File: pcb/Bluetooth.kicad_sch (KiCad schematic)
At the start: 17 parts, among them U13 RN4678, U14 TXB0102DCU

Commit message: [pcb] Footprints assigned
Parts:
- C26: footprint (none) -> Capacitor_Tantalum_SMD:CP_EIA-3216-18_Kemet-A
- C27, C28, C29: footprint (none) -> Capacitor_SMD:C_0805_2012Metric
- D8: footprint (none) -> LED_SMD:LED_0805_2012Metric
- JP1, JP2, JP3, JP4, JP5, JP6: footprint (none) -> Connector_PinHeader_2.54mm:PinHeader_1x02_P2.54mm_Vertical
- R38, R39: footprint (none) -> Resistor_SMD:R_0805_2012Metric
- TP18, TP19: footprint (none) -> TestPoint:TestPoint_Pad_D2.0mm
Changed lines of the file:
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@@
       (effects (font (size 1.27 1.27)) hide)
     )
-    (property "Footprint" "" (at 93.98 64.77 0)
+    (property "Footprint" "Connector_PinHeader_2.54mm:PinHeader_1x02_P2.54mm_Vertical" (at 93.98 64.77 0)
       (effects (font (size 1.27 1.27)) hide)
     )
@@
       (effects (font (size 1.27 1.27)) (justify right) hide)
     )
-    (property "Footprint" "" (at 64.77 93.98 0)
+    (property "Footprint" "Connector_PinHeader_2.54mm:PinHeader_1x02_P2.54mm_Vertical" (at 64.77 93.98 0)
       (effects (font (size 1.27 1.27)) hide)
     )
@@
       (effects (font (size 1.27 1.27)) hide)
     )
-    (property "Footprint" "" (at 182.88 68.58 0)
+    (property "Footprint" "Connector_PinHeader_2.54mm:PinHeader_1x02_P2.54mm_Vertical" (at 182.88 68.58 0)
       (effects (font (size 1.27 1.27)) hide)
     )
@@
       (effects (font (size 1.27 1.27)) (justify right))
     )
-    (property "Footprint" "" (at 140.6652 53.34 0)
+    (property "Footprint" "Capacitor_SMD:C_0805_2012Metric" (at 140.6652 53.34 0)
       (effects (font (size 1.27 1.27)) hide)
     )
@@
       (effects (font (size 1.27 1.27)))
     )
-    (property "Footprint" "" (at 93.98 52.07 0)
+    (property "Footprint" "LED_SMD:LED_0805_2012Metric" (at 93.98 52.07 0)
       (effects (font (size 1.27 1.27)) hide)
     )
@@
       (effects (font (size 1.27 1.27)) (justify right) hide)
     )
-    (property "Footprint" "" (at 67.31 93.98 0)
+    (property "Footprint" "Connector_PinHeader_2.54mm:PinHeader_1x02_P2.54mm_Vertical" (at 67.31 93.98 0)
       (effects (font (size 1.27 1.27)) hide)
     )
@@
       (effects (font (size 1.27 1.27)) (justify left))
     )
-    (property "Footprint" "" (at 91.1352 104.14 0)
+    (property "Footprint" "Capacitor_SMD:C_0805_2012Metric" (at 91.1352 104.14 0)
       (effects (font (size 1.27 1.27)) hide)
     )
@@
       (effects (font (size 1.27 1.27)) (justify left) hide)
     )
-    (property "Footprint" "" (at 181.61 67.31 0)
+    (property "Footprint" "TestPoint:TestPoint_Pad_D2.0mm" (at 181.61 67.31 0)
       (effects (font (size 1.27 1.27)) hide)
     )
@@
       (effects (font (size 1.27 1.27)) (justify left))
     )
-    (property "Footprint" "" (at 168.6052 60.96 0)
+    (property "Footprint" "Capacitor_SMD:C_0805_2012Metric" (at 168.6052 60.96 0)
       (effects (font (size 1.27 1.27)) hide)
     )
@@
       (effects (font (size 1.27 1.27)))
     )
-    (property "Footprint" "" (at 50.8 93.218 90)
+    (property "Footprint" "Resistor_SMD:R_0805_2012Metric" (at 50.8 93.218 90)
       (effects (font (size 1.27 1.27)) hide)
     )
@@
       (effects (font (size 1.27 1.27)) (justify left) hide)
     )
-    (property "Footprint" "" (at 171.45 74.93 0)
+    (property "Footprint" "TestPoint:TestPoint_Pad_D2.0mm" (at 171.45 74.93 0)
       (effects (font (size 1.27 1.27)) hide)
     )
@@
       (effects (font (size 1.27 1.27)) (justify left))
     )
-    (property "Footprint" "" (at 88.392 90.17 90)
+    (property "Footprint" "Resistor_SMD:R_0805_2012Metric" (at 88.392 90.17 90)
       (effects (font (size 1.27 1.27)) hide)
     )
@@
       (effects (font (size 1.27 1.27)) hide)
     )
-    (property "Footprint" "" (at 182.88 73.66 0)
+    (property "Footprint" "Connector_PinHeader_2.54mm:PinHeader_1x02_P2.54mm_Vertical" (at 182.88 73.66 0)
       (effects (font (size 1.27 1.27)) hide)
     )
@@
       (effects (font (size 1.27 1.27)) (justify right) hide)
     )
-    (property "Footprint" "" (at 69.85 93.98 0)
+    (property "Footprint" "Connector_PinHeader_2.54mm:PinHeader_1x02_P2.54mm_Vertical" (at 69.85 93.98 0)
       (effects (font (size 1.27 1.27)) hide)
     )
@@
       (effects (font (size 1.27 1.27)) (justify left))
     )
-    (property "Footprint" "" (at 26.9748 55.88 0)
-      (effects (font (size 1.27 1.27)) hide)
-    )
+    (property "Footprint" "Capacitor_Tantalum_SMD:CP_EIA-3216-18_Kemet-A" (at 26.9748 55.88 0)
+      (effects (font (size 1.27 1.27)) hide)
+    )

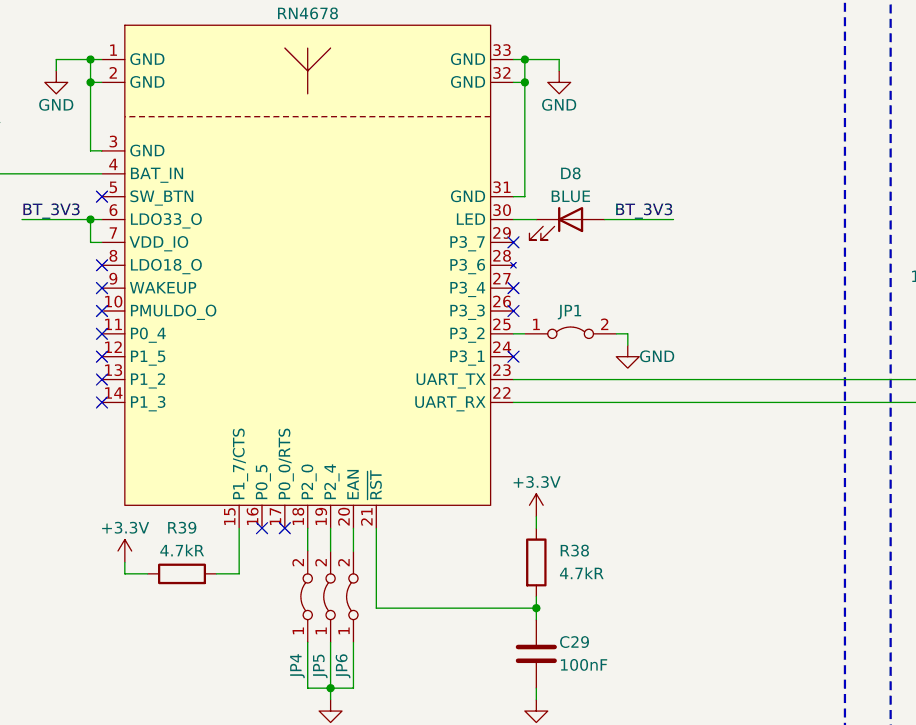
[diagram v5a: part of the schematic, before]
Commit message: [pcb] Add 100R resistor for BT status LED
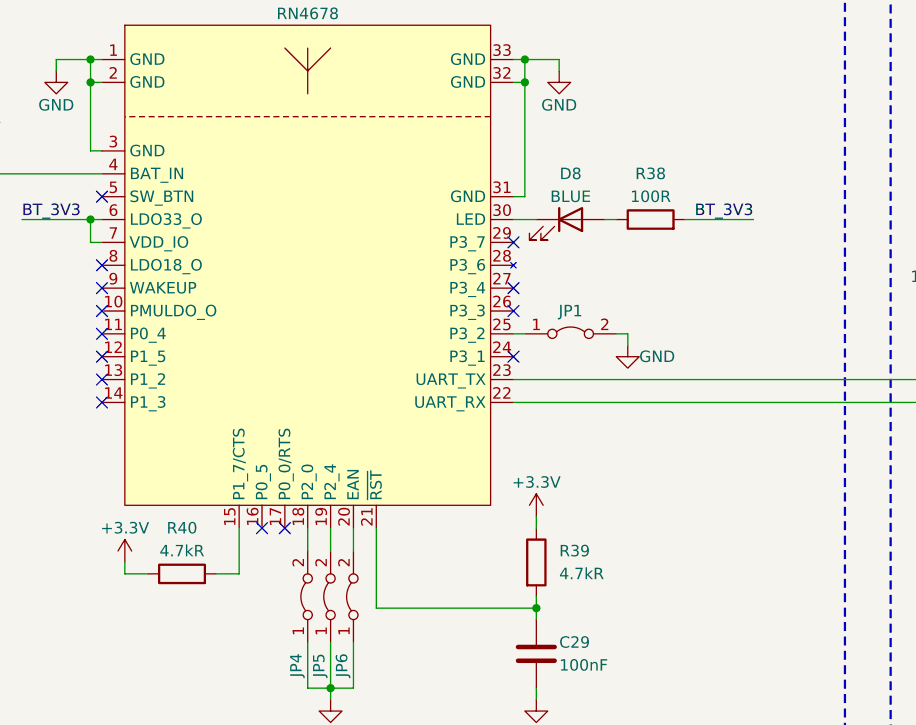
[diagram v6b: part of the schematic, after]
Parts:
- added R38: 100R, Resistor_SMD:R_0805_2012Metric, symbol Device:R
- renumbered R38 to R39, R39 to R40
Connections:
- net BT_3V3: now also R38.2; no longer D8.2 (A)
- new net: D8.2 (A), R38.1
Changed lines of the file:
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@@
+    (stroke (width 0) (type default))
+  )
+  (wire (pts (xy 106.68 52.07) (xy 114.3 52.07))
     (stroke (width 0) (type default))
   )
@@
     (stroke (width 0) (type default))
   )
-  (wire (pts (xy 97.79 52.07) (xy 105.41 52.07))
-    (stroke (width 0) (type default))
-  )
   (wire (pts (xy 36.83 35.56) (xy 36.83 34.29))
     (stroke (width 0) (type default))
@@
   )
   (wire (pts (xy 87.63 49.53) (xy 88.9 49.53))
+    (stroke (width 0) (type default))
+  )
+  (wire (pts (xy 97.79 52.07) (xy 99.06 52.07))
     (stroke (width 0) (type default))
   )
@@
     (effects (font (size 2 2) (thickness 0.4) bold) (justify left bottom))
   )
-  (label "BT_3V3" (at 105.41 52.07 180) (fields_autoplaced)
+  (label "BT_3V3" (at 114.3 52.07 180) (fields_autoplaced)
     (effects (font (size 1.27 1.27)) (justify right bottom))
   )
@@
     )
   )
+  (symbol (lib_id "Device:R") (at 102.87 52.07 90) (unit 1)
+    (in_bom yes) (on_board yes) (dnp no)
+    (property "Reference" "R38" (at 102.87 46.99 90)
+      (effects (font (size 1.27 1.27)))
+    )
+    (property "Value" "100R" (at 102.87 49.53 90)
+      (effects (font (size 1.27 1.27)))
+    )
+    (property "Footprint" "Resistor_SMD:R_0805_2012Metric" (at 102.87 53.848 90)
+      (effects (font (size 1.27 1.27)) hide)
+    )
+    (property "Datasheet" "~" (at 102.87 52.07 0)
+      (effects (font (size 1.27 1.27)) hide)
+    )
+    (pin "1")
+    (pin "2")
+    (instances
+      (project "Autko"
+        (path "/8d5cfdec-de34-4148-9100-7125640c46f5/bb9a200c-6921-438f-a82b-708524bb5612"
+          (reference "R38") (unit 1)
+        )
+      )
+    )
+  )
   (symbol (lib_id "power:GND") (at 139.7 62.23 0) (unit 1)
     (in_bom yes) (on_board yes) (dnp no)
@@
   (symbol (lib_id "Device:R") (at 50.8 91.44 90) (unit 1)
     (in_bom yes) (on_board yes) (dnp no)
-    (property "Reference" "R39" (at 50.8 86.36 90)
+    (property "Reference" "R40" (at 50.8 86.36 90)
       (effects (font (size 1.27 1.27)))
     )
@@
       (project "Autko"
         (path "/8d5cfdec-de34-4148-9100-7125640c46f5/bb9a200c-6921-438f-a82b-708524bb5612"
-          (reference "R39") (unit 1)
+          (reference "R40") (unit 1)
         )
       )
@@
   (symbol (lib_id "Device:R") (at 90.17 90.17 0) (unit 1)
     (in_bom yes) (on_board yes) (dnp no)
-    (property "Reference" "R38" (at 92.71 88.9 0)
+    (property "Reference" "R39" (at 92.71 88.9 0)
       (effects (font (size 1.27 1.27)) (justify left))
     )
@@
       (project "Autko"
         (path "/8d5cfdec-de34-4148-9100-7125640c46f5/bb9a200c-6921-438f-a82b-708524bb5612"
-          (reference "R38") (unit 1)
-        )
-      )
+          (reference "R39") (unit 1)
+        )
+      )

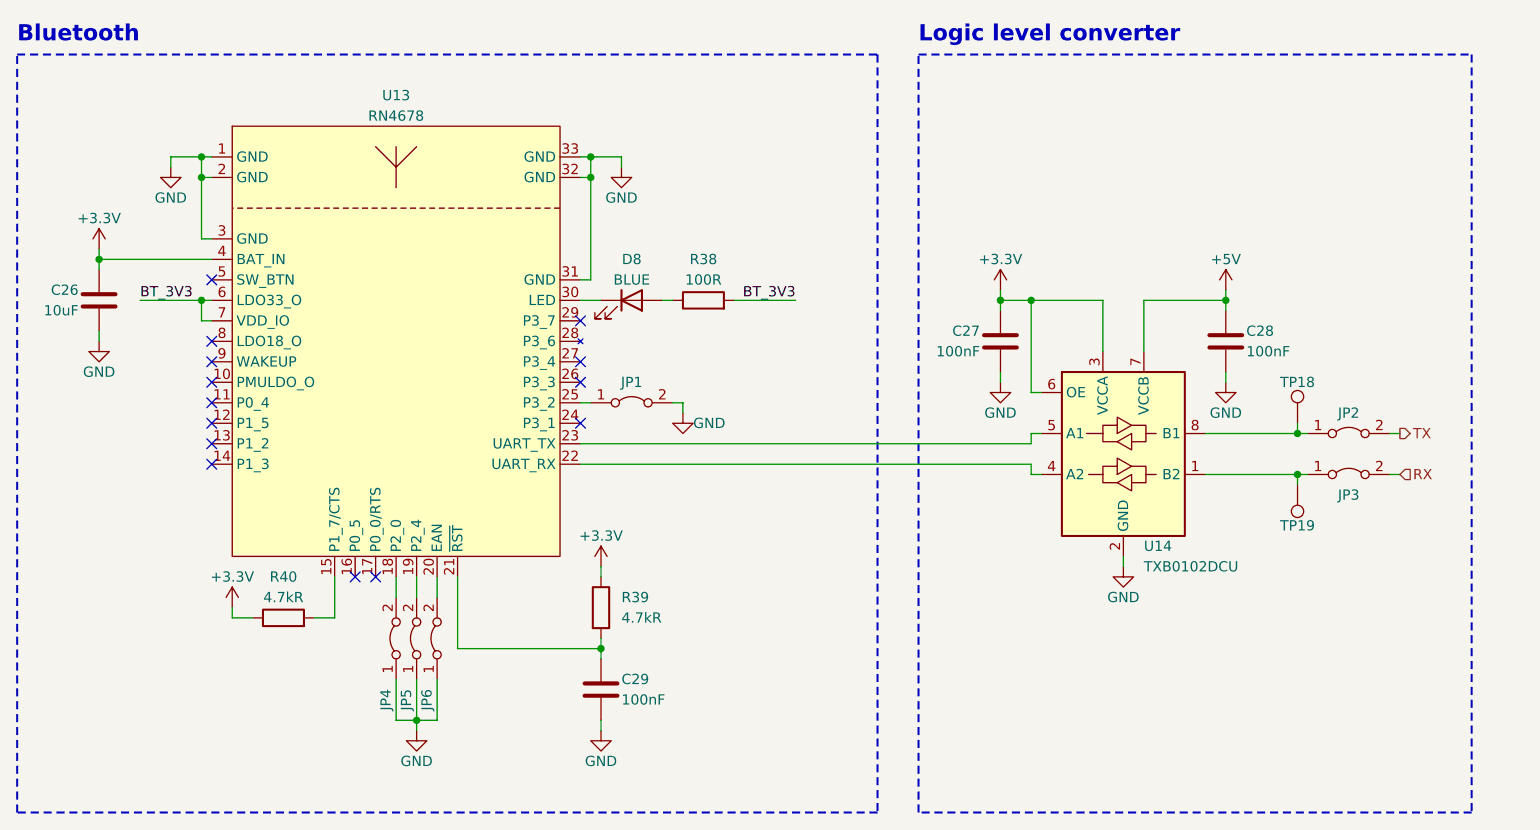
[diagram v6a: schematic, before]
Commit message: [pcb] Rework schematic for ATxmega16A4U
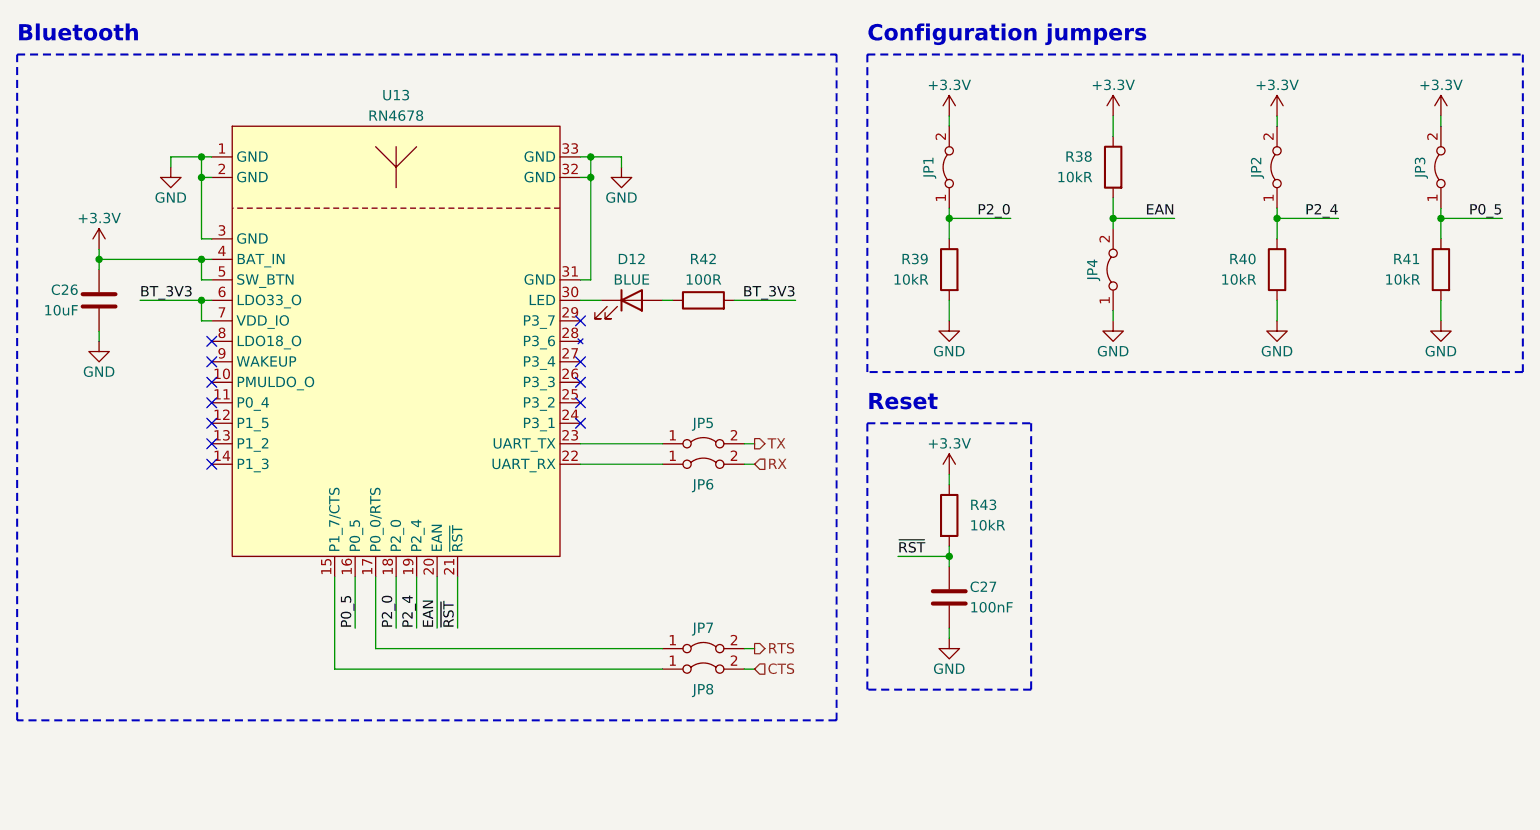
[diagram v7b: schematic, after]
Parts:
- removed C27, C28: 100nF, Capacitor_SMD:C_0805_2012Metric, symbol Device:C
- removed JP5, JP6: Jumper_2_Bridged, Connector_PinHeader_2.54mm:PinHeader_1x02_P2.54mm_Vertical, symbol Jumper:Jumper_2_Bridged
- removed TP18, TP19: TestPoint, TestPoint:TestPoint_Pad_D2.0mm, symbol Connector:TestPoint
- removed U14: TXB0102DCU, Package_SO:VSSOP-8_2.4x2.1mm_P0.5mm, symbol Logic_LevelTranslator:TXB0102DCU
- added JP2, JP3, JP7, JP8: Jumper_2_Bridged, Connector_PinHeader_2.54mm:PinHeader_1x02_P2.54mm_Vertical, symbol Jumper:Jumper_2_Bridged
- added R38, R39, R41: 10kR, Resistor_SMD:R_0805_2012Metric, symbol Device:R
- R40: value 4.7kR -> 10kR
- R43: renamed from R39; value 4.7kR -> 10kR
- renumbered C29 to C27, D8 to D12, JP2 to JP5, JP3 to JP6, R38 to R42
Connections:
- net +3.3V: now also JP1.2 (B), U13.5 (SW_BTN), JP2.2 (B), JP3.2 (B), R38.1; no longer R40.1
- net GND: now also R40.2, R39.2, R41.2; no longer JP1.2 (B)
- net at U13.25 (P3_2): no longer JP1.1 (A)
- net at U13.15 (P1_7/CTS): now also JP8.1 (A); no longer R40.2
- net P0_5: now reaches U13.16 (P0_5)
- net P0_5: now also JP3.1 (A), R41.1
- net at U13.17 (P0_0/RTS): now also JP7.1 (A)
- net EAN: now reaches JP4.2 (B)
- net EAN: now also U13.20 (EAN), R38.2; no longer U13.18 (P2_0)
- net P2_4: now reaches U13.19 (P2_4)
- net P2_4: now also R40.1, JP2.1 (A)
- net ~{RST}: now reaches C27.1, R43.2, U13.21 (~{RST})
- net at U13.22 (UART_RX): now also JP6.1 (A)
- net at U13.23 (UART_TX): now also JP5.1 (A)
- new net CTS: JP8.2 (B)
- new net P2_0: JP1.1 (A), R39.1, U13.18 (P2_0)
- new net RTS: JP7.2 (B)
- no-connect marks 14 -> 12
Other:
- note added: "Configuration jumpers"
- note added: "Reset"
- note removed: "Logic level converter"
- moved on the sheet: C27, JP1, JP5, JP6, R43

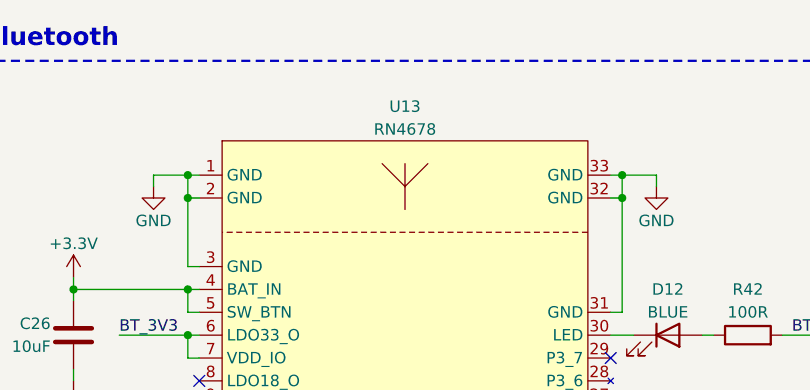
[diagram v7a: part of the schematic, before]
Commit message: Power switch footprint and initial pcb
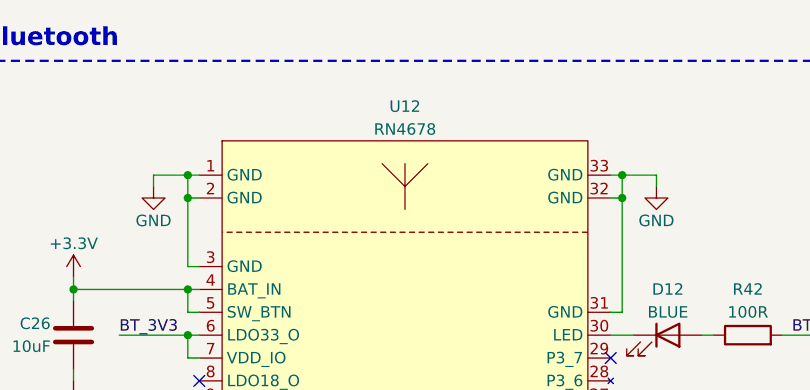
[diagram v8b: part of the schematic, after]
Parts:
- renumbered U13 to U12
